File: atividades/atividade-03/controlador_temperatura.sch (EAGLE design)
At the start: 23 parts, among them Q1 BC337, Q2 BC337, Q3 BC337

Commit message: buttons scheme
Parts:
- added R10, R11, R8, R9: 10k, resistor-power:RRS1/8
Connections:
- new net N$10: BUTTONS.5, R8.2
- new net N$11: BUTTONS.4, R9.2
- new net N$12: BUTTONS.3, R10.2
- new net N$13: BUTTONS.2, R11.2
- net GND: now also BUTTONS.1, BUTTONS.6
- net VCC: now also R10.1, R11.1, R8.1, R9.1
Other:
- moved on the sheet: BUTTONS
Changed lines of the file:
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@@
 <part name="RST" library="con-amp" library_urn="urn:adsk.eagle:library:127" deviceset="MTA02-100" device="" package3d_urn="urn:adsk.eagle:package:8081649/1"/>
 <part name="GND7" library="supply1" library_urn="urn:adsk.eagle:library:371" deviceset="GND" device=""/>
+<part name="R8" library="resistor-power" library_urn="urn:adsk.eagle:library:344" deviceset="R" device="RS1/8" package3d_urn="urn:adsk.eagle:package:25168/1" value="10k"/>
+<part name="R9" library="resistor-power" library_urn="urn:adsk.eagle:library:344" deviceset="R" device="RS1/8" package3d_urn="urn:adsk.eagle:package:25168/1" value="10k"/>
+<part name="R10" library="resistor-power" library_urn="urn:adsk.eagle:library:344" deviceset="R" device="RS1/8" package3d_urn="urn:adsk.eagle:package:25168/1" value="10k"/>
+<part name="R11" library="resistor-power" library_urn="urn:adsk.eagle:library:344" deviceset="R" device="RS1/8" package3d_urn="urn:adsk.eagle:package:25168/1" value="10k"/>
+<part name="GND8" library="supply1" library_urn="urn:adsk.eagle:library:371" deviceset="GND" device=""/>
+<part name="GND9" library="supply1" library_urn="urn:adsk.eagle:library:371" deviceset="GND" device=""/>
 </parts>
 <sheets>
@@
 <attribute name="NAME" x="193.548" y="-28.829" size="1.778" layer="95"/>
 </instance>
-<instance part="P+1" gate="VCC" x="190.5" y="68.58" smashed="yes">
-<attribute name="VALUE" x="187.96" y="66.04" size="1.778" layer="96" rot="R90"/>
+<instance part="P+1" gate="VCC" x="185.42" y="43.18" smashed="yes">
+<attribute name="VALUE" x="182.88" y="40.64" size="1.778" layer="96" rot="R90"/>
 </instance>
 <instance part="R2" gate="G$1" x="-30.48" y="38.1" smashed="yes" rot="R180">
@@
 <attribute name="VALUE" x="13.97" y="30.861" size="1.778" layer="96" rot="R180"/>
 </instance>
-<instance part="BUTTONS" gate="G$1" x="185.42" y="53.34" smashed="yes">
-<attribute name="NAME" x="195.58" y="50.8" size="1.778" layer="95"/>
-<attribute name="VALUE" x="200.66" y="49.53" size="1.778" layer="96"/>
+<instance part="BUTTONS" gate="G$1" x="162.56" y="50.8" smashed="yes">
+<attribute name="NAME" x="172.72" y="48.26" size="1.778" layer="95"/>
+<attribute name="VALUE" x="177.8" y="46.99" size="1.778" layer="96"/>
 </instance>
 <instance part="HTR_LED" gate="G$1" x="25.4" y="30.48" smashed="yes" rot="R270">
@@
 <instance part="GND7" gate="1" x="91.44" y="-43.18" smashed="yes" rot="R270">
 <attribute name="VALUE" x="88.9" y="-40.64" size="1.778" layer="96" rot="R270"/>
+</instance>
+<instance part="R8" gate="G$1" x="177.8" y="35.56" smashed="yes" rot="R180">
+<attribute name="NAME" x="181.61" y="34.1884" size="1.778" layer="95" rot="R180"/>
+<attribute name="VALUE" x="181.61" y="38.481" size="1.778" layer="96" rot="R180"/>
+</instance>
+<instance part="R9" gate="G$1" x="177.8" y="27.94" smashed="yes" rot="R180">
+<attribute name="NAME" x="181.61" y="26.5684" size="1.778" layer="95" rot="R180"/>
+<attribute name="VALUE" x="181.61" y="30.861" size="1.778" layer="96" rot="R180"/>
+</instance>
+<instance part="R10" gate="G$1" x="177.8" y="20.32" smashed="yes" rot="R180">
+<attribute name="NAME" x="181.61" y="18.9484" size="1.778" layer="95" rot="R180"/>
+<attribute name="VALUE" x="181.61" y="23.241" size="1.778" layer="96" rot="R180"/>
+</instance>
+<instance part="R11" gate="G$1" x="177.8" y="12.7" smashed="yes" rot="R180">
+<attribute name="NAME" x="181.61" y="11.3284" size="1.778" layer="95" rot="R180"/>
+<attribute name="VALUE" x="181.61" y="15.621" size="1.778" layer="96" rot="R180"/>
+</instance>
+<instance part="GND8" gate="1" x="154.94" y="43.18" smashed="yes" rot="R270">
+<attribute name="VALUE" x="152.4" y="45.72" size="1.778" layer="96" rot="R270"/>
+</instance>
+<instance part="GND9" gate="1" x="172.72" y="43.18" smashed="yes" rot="R90">
+<attribute name="VALUE" x="175.26" y="40.64" size="1.778" layer="96" rot="R90"/>
 </instance>
 </instances>
@@
 <wire x1="93.98" y1="-43.18" x2="101.6" y2="-43.18" width="0.1524" layer="91"/>
 </segment>
+<segment>
+<pinref part="GND8" gate="1" pin="GND"/>
+<pinref part="BUTTONS" gate="G$1" pin="1"/>
+<wire x1="157.48" y1="43.18" x2="157.48" y2="48.26" width="0.1524" layer="91"/>
+</segment>
+<segment>
+<pinref part="BUTTONS" gate="G$1" pin="6"/>
+<pinref part="GND9" gate="1" pin="GND"/>
+<wire x1="170.18" y1="48.26" x2="170.18" y2="43.18" width="0.1524" layer="91"/>
+</segment>
 </net>
 <net name="N$1" class="0">
@@
 <wire x1="76.2" y1="17.78" x2="78.74" y2="17.78" width="0.1524" layer="91"/>
 </segment>
+<segment>
+<pinref part="R11" gate="G$1" pin="1"/>
+<wire x1="182.88" y1="12.7" x2="185.42" y2="12.7" width="0.1524" layer="91"/>
+<pinref part="R10" gate="G$1" pin="1"/>
+<wire x1="182.88" y1="20.32" x2="185.42" y2="20.32" width="0.1524" layer="91"/>
+<wire x1="185.42" y1="12.7" x2="185.42" y2="20.32" width="0.1524" layer="91"/>
+<pinref part="R9" gate="G$1" pin="1"/>
+<wire x1="185.42" y1="27.94" x2="182.88" y2="27.94" width="0.1524" layer="91"/>
+<wire x1="185.42" y1="20.32" x2="185.42" y2="27.94" width="0.1524" layer="91"/>
+<junction x="185.42" y="20.32"/>
+<pinref part="R8" gate="G$1" pin="1"/>
+<wire x1="182.88" y1="35.56" x2="185.42" y2="35.56" width="0.1524" layer="91"/>
+<wire x1="185.42" y1="27.94" x2="185.42" y2="35.56" width="0.1524" layer="91"/>
+<junction x="185.42" y="27.94"/>
+<pinref part="P+1" gate="VCC" pin="VCC"/>
+<wire x1="185.42" y1="35.56" x2="185.42" y2="40.64" width="0.1524" layer="91"/>
+<junction x="185.42" y="35.56"/>
+</segment>
 </net>
 <net name="A5" class="0">
@@
 </segment>
 </net>
+<net name="N$10" class="0">
+<segment>
+<pinref part="BUTTONS" gate="G$1" pin="5"/>
+<wire x1="167.64" y1="48.26" x2="167.64" y2="35.56" width="0.1524" layer="91"/>
+<pinref part="R8" gate="G$1" pin="2"/>
+<wire x1="167.64" y1="35.56" x2="172.72" y2="35.56" width="0.1524" layer="91"/>
+</segment>
+</net>
+<net name="N$11" class="0">
+<segment>
+<pinref part="R9" gate="G$1" pin="2"/>
+<wire x1="172.72" y1="27.94" x2="165.1" y2="27.94" width="0.1524" layer="91"/>
+<pinref part="BUTTONS" gate="G$1" pin="4"/>
+<wire x1="165.1" y1="27.94" x2="165.1" y2="48.26" width="0.1524" layer="91"/>
+</segment>
+</net>
+<net name="N$12" class="0">
+<segment>
+<pinref part="R10" gate="G$1" pin="2"/>
+<wire x1="172.72" y1="20.32" x2="162.56" y2="20.32" width="0.1524" layer="91"/>
+<pinref part="BUTTONS" gate="G$1" pin="3"/>
+<wire x1="162.56" y1="20.32" x2="162.56" y2="48.26" width="0.1524" layer="91"/>
+</segment>
+</net>
+<net name="N$13" class="0">
+<segment>
+<pinref part="R11" gate="G$1" pin="2"/>
+<wire x1="172.72" y1="12.7" x2="160.02" y2="12.7" width="0.1524" layer="91"/>
+<pinref part="BUTTONS" gate="G$1" pin="2"/>
+<wire x1="160.02" y1="12.7" x2="160.02" y2="48.26" width="0.1524" layer="91"/>
+</segment>
+</net>

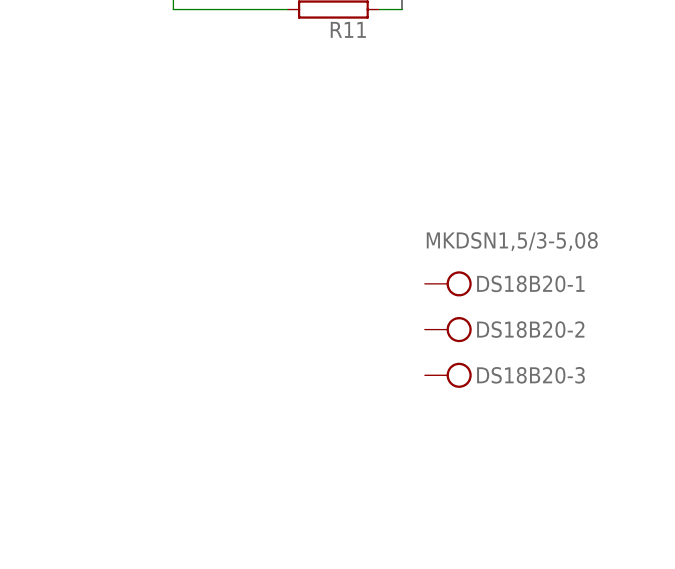
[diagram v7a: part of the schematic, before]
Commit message: oneWire buss cheme
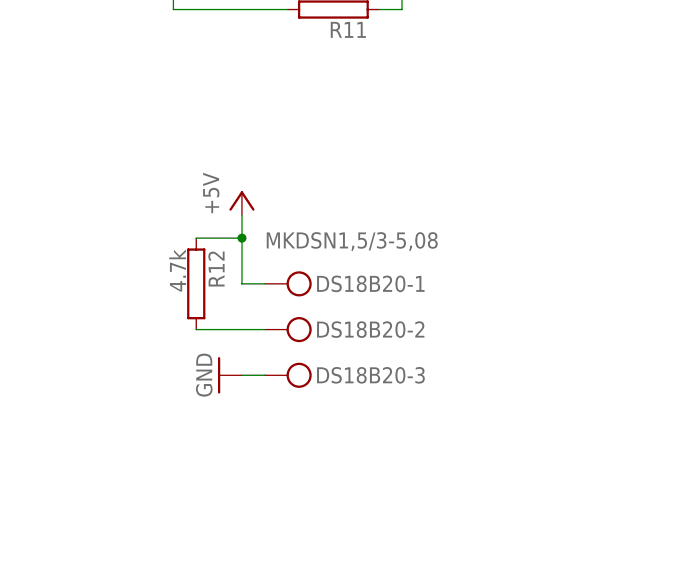
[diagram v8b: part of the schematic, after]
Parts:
- added R12: 4.7k, resistor-power:RRS1/8
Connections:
- new net N$15: DS18B20-2.KL, R12.2
- net GND: now also DS18B20-3.KL
- net VCC: now also DS18B20-1.KL, R12.1
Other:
- moved on the sheet: DS18B20-1, DS18B20-2, DS18B20-3
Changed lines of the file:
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@@
 <part name="GND8" library="supply1" library_urn="urn:adsk.eagle:library:371" deviceset="GND" device=""/>
 <part name="GND9" library="supply1" library_urn="urn:adsk.eagle:library:371" deviceset="GND" device=""/>
+<part name="P+5" library="supply1" library_urn="urn:adsk.eagle:library:371" deviceset="VCC" device="" value="+5V"/>
+<part name="R12" library="resistor-power" library_urn="urn:adsk.eagle:library:344" deviceset="R" device="RS1/8" package3d_urn="urn:adsk.eagle:package:25168/1" value="4.7k"/>
+<part name="GND10" library="supply1" library_urn="urn:adsk.eagle:library:371" deviceset="GND" device=""/>
 </parts>
 <sheets>
@@
 <attribute name="VALUE" x="20.32" y="34.417" size="1.778" layer="96"/>
 </instance>
-<instance part="DS18B20" gate="-1" x="190.5" y="-17.78" smashed="yes">
-<attribute name="NAME" x="193.548" y="-18.669" size="1.778" layer="95"/>
-<attribute name="VALUE" x="187.96" y="-13.843" size="1.778" layer="96"/>
-</instance>
-<instance part="DS18B20" gate="-2" x="190.5" y="-22.86" smashed="yes">
-<attribute name="NAME" x="193.548" y="-23.749" size="1.778" layer="95"/>
-</instance>
-<instance part="DS18B20" gate="-3" x="190.5" y="-27.94" smashed="yes">
-<attribute name="NAME" x="193.548" y="-28.829" size="1.778" layer="95"/>
+<instance part="DS18B20" gate="-1" x="172.72" y="-17.78" smashed="yes">
+<attribute name="NAME" x="175.768" y="-18.669" size="1.778" layer="95"/>
+<attribute name="VALUE" x="170.18" y="-13.843" size="1.778" layer="96"/>
+</instance>
+<instance part="DS18B20" gate="-2" x="172.72" y="-22.86" smashed="yes">
+<attribute name="NAME" x="175.768" y="-23.749" size="1.778" layer="95"/>
+</instance>
+<instance part="DS18B20" gate="-3" x="172.72" y="-27.94" smashed="yes">
+<attribute name="NAME" x="175.768" y="-28.829" size="1.778" layer="95"/>
 </instance>
 <instance part="P+1" gate="VCC" x="185.42" y="43.18" smashed="yes">
@@
 <instance part="GND9" gate="1" x="172.72" y="43.18" smashed="yes" rot="R90">
 <attribute name="VALUE" x="175.26" y="40.64" size="1.778" layer="96" rot="R90"/>
+</instance>
+<instance part="P+5" gate="VCC" x="167.64" y="-7.62" smashed="yes">
+<attribute name="VALUE" x="165.1" y="-10.16" size="1.778" layer="96" rot="R90"/>
+</instance>
+<instance part="R12" gate="G$1" x="162.56" y="-17.78" smashed="yes" rot="R270">
+<attribute name="NAME" x="163.9316" y="-13.97" size="1.778" layer="95" rot="R270"/>
+<attribute name="VALUE" x="159.639" y="-13.97" size="1.778" layer="96" rot="R270"/>
+</instance>
+<instance part="GND10" gate="1" x="165.1" y="-27.94" smashed="yes" rot="R270">
+<attribute name="VALUE" x="162.56" y="-25.4" size="1.778" layer="96" rot="R270"/>
 </instance>
 </instances>
@@
 <wire x1="170.18" y1="48.26" x2="170.18" y2="43.18" width="0.1524" layer="91"/>
 </segment>
+<segment>
+<pinref part="DS18B20" gate="-3" pin="KL"/>
+<pinref part="GND10" gate="1" pin="GND"/>
+<wire x1="170.18" y1="-27.94" x2="167.64" y2="-27.94" width="0.1524" layer="91"/>
+</segment>
 </net>
 <net name="N$1" class="0">
@@
 <junction x="185.42" y="35.56"/>
 </segment>
+<segment>
+<pinref part="P+5" gate="VCC" pin="VCC"/>
+<wire x1="167.64" y1="-10.16" x2="167.64" y2="-12.7" width="0.1524" layer="91"/>
+<pinref part="DS18B20" gate="-1" pin="KL"/>
+<wire x1="167.64" y1="-12.7" x2="167.64" y2="-17.78" width="0.1524" layer="91"/>
+<wire x1="167.64" y1="-17.78" x2="170.18" y2="-17.78" width="0.1524" layer="91"/>
+<pinref part="R12" gate="G$1" pin="1"/>
+<wire x1="162.56" y1="-12.7" x2="167.64" y2="-12.7" width="0.1524" layer="91"/>
+<junction x="167.64" y="-12.7"/>
+</segment>
 </net>
 <net name="A5" class="0">
@@
 </segment>
 </net>
+<net name="N$15" class="0">
+<segment>
+<pinref part="DS18B20" gate="-2" pin="KL"/>
+<pinref part="R12" gate="G$1" pin="2"/>
+<wire x1="170.18" y1="-22.86" x2="162.56" y2="-22.86" width="0.1524" layer="91"/>
+</segment>
+</net>
